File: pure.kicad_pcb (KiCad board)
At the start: 2 copper layers, 100 x 90 mm, 46 parts, among them K1 G5V-2_Split, Q1 DTC143Z, U1 SN74LVC1G3157DBVR, U2 SN74LVC1G3157DBVR, U3 74HC4053, U4 74HC4053, U5 MC33079

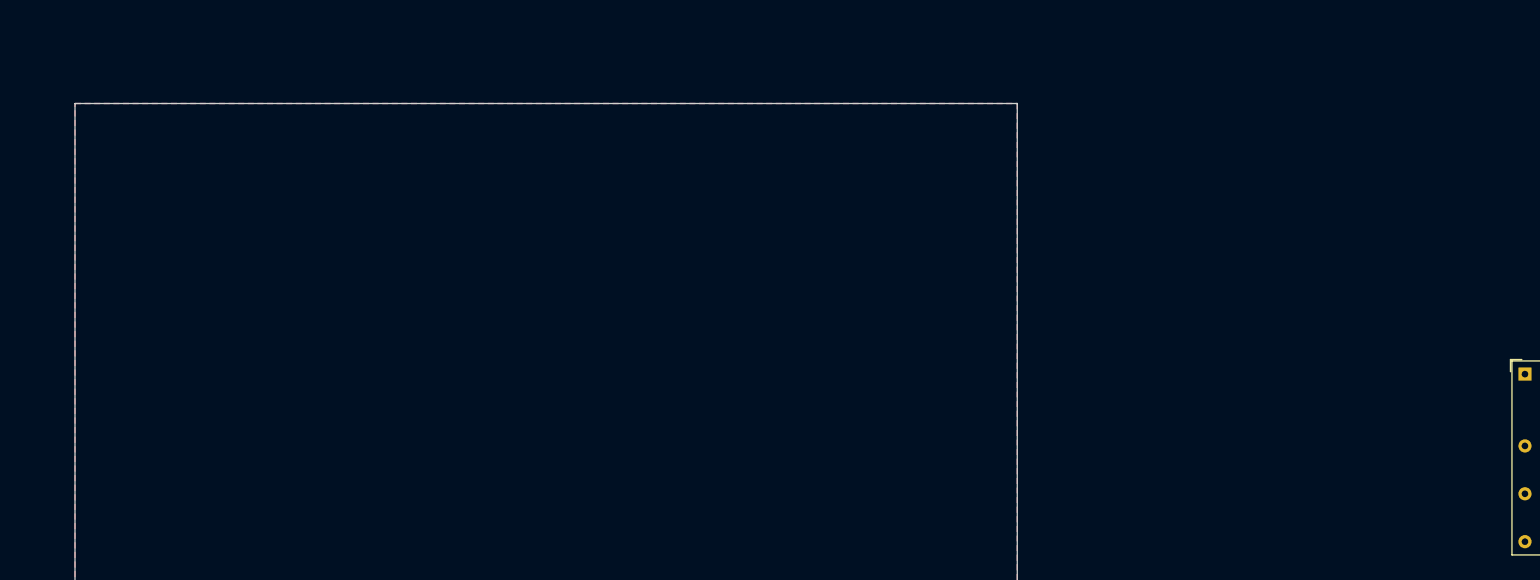
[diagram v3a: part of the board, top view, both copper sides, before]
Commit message: finich IF_RX_Schematics, begin MCU, delete *.sch files
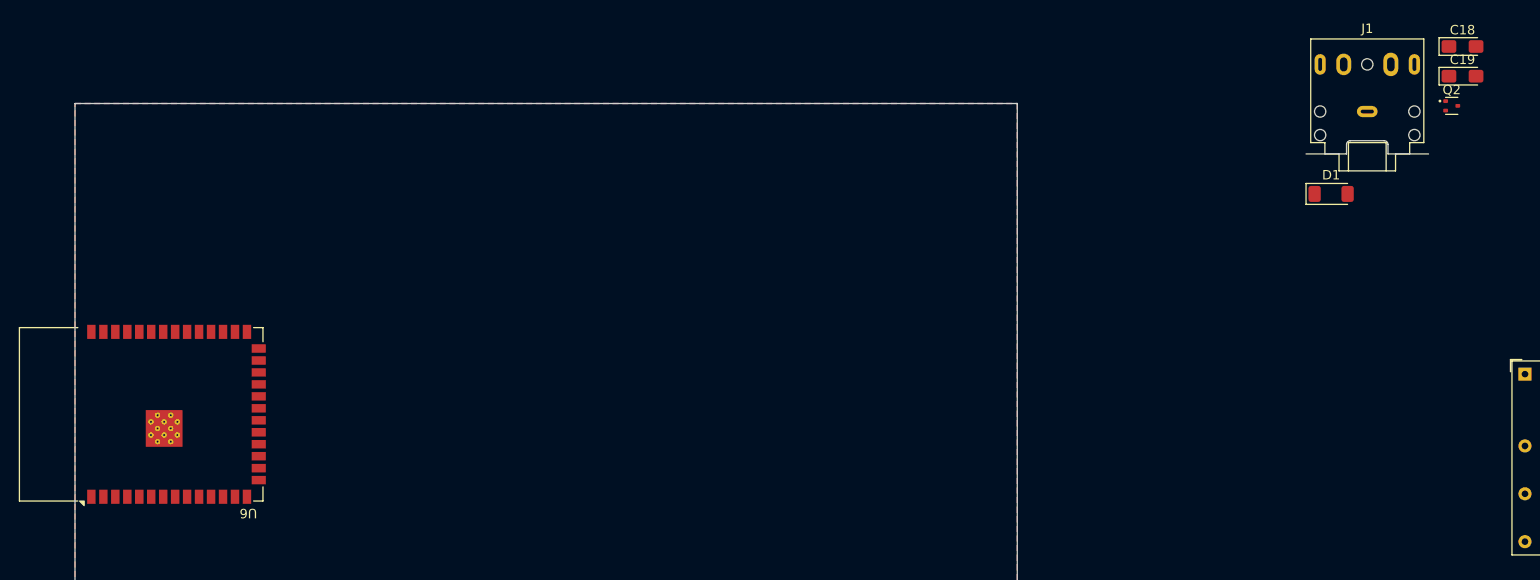
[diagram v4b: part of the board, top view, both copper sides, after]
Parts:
- added C18: 10uF, Capacitor_Tantalum_SMD:CP_EIA-3216-18_Kemet-A_Pad1.58x1.35mm_HandSolder, F.Cu at (212.2, 34.0)
- added C19: 10uF, Capacitor_Tantalum_SMD:CP_EIA-3216-18_Kemet-A_Pad1.58x1.35mm_HandSolder, F.Cu at (212.2, 37.1)
- added D1: LL4148, Diode_SMD:D_MiniMELF, F.Cu at (198.3, 49.6)
- added J1: LINE_IN, Connector_Audio:Jack_3.5mm_CUI_SJ1-3525N_Horizontal, F.Cu at (202.1, 40.9)
- added Q2: DTC143Z, Package_TO_SOT_SMD:SOT-523, F.Cu at (211.1, 40.2)
- added U6: ESP32-S3-WROOM-1, RF_Module:ESP32-S3-WROOM-1, F.Cu at (72.0, 73.0)
- K1: value G5V-2_Split -> RS-12
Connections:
- net Net-(R18-Pad1) renamed R_LINE_IN
- net Net-(R8-Pad2) renamed L_LINE_IN
- K1 pad 1: unconnected-(K1-Pad1) -> +12V
- K1 pad 16: unconnected-(K1-Pad16) -> Net-(D1-A)

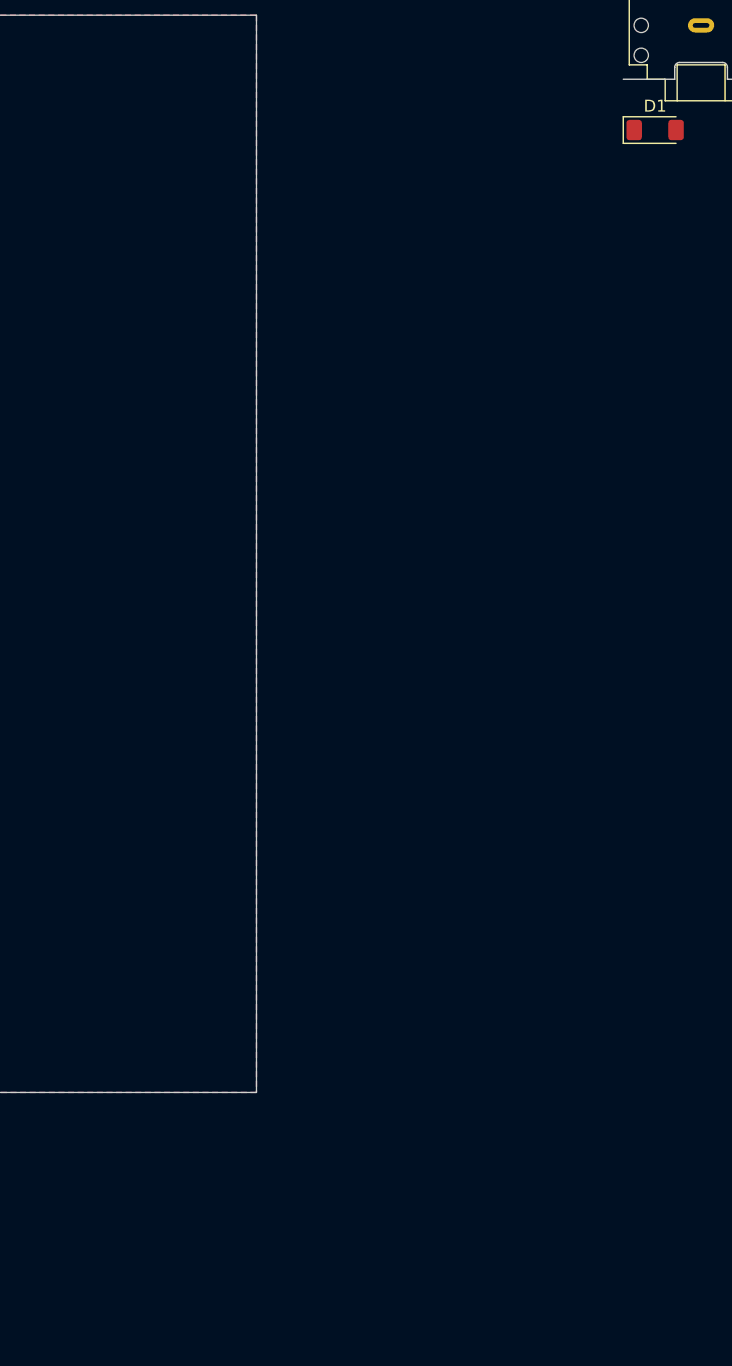
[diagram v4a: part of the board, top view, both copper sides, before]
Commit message: schematics mixer progress, mcu
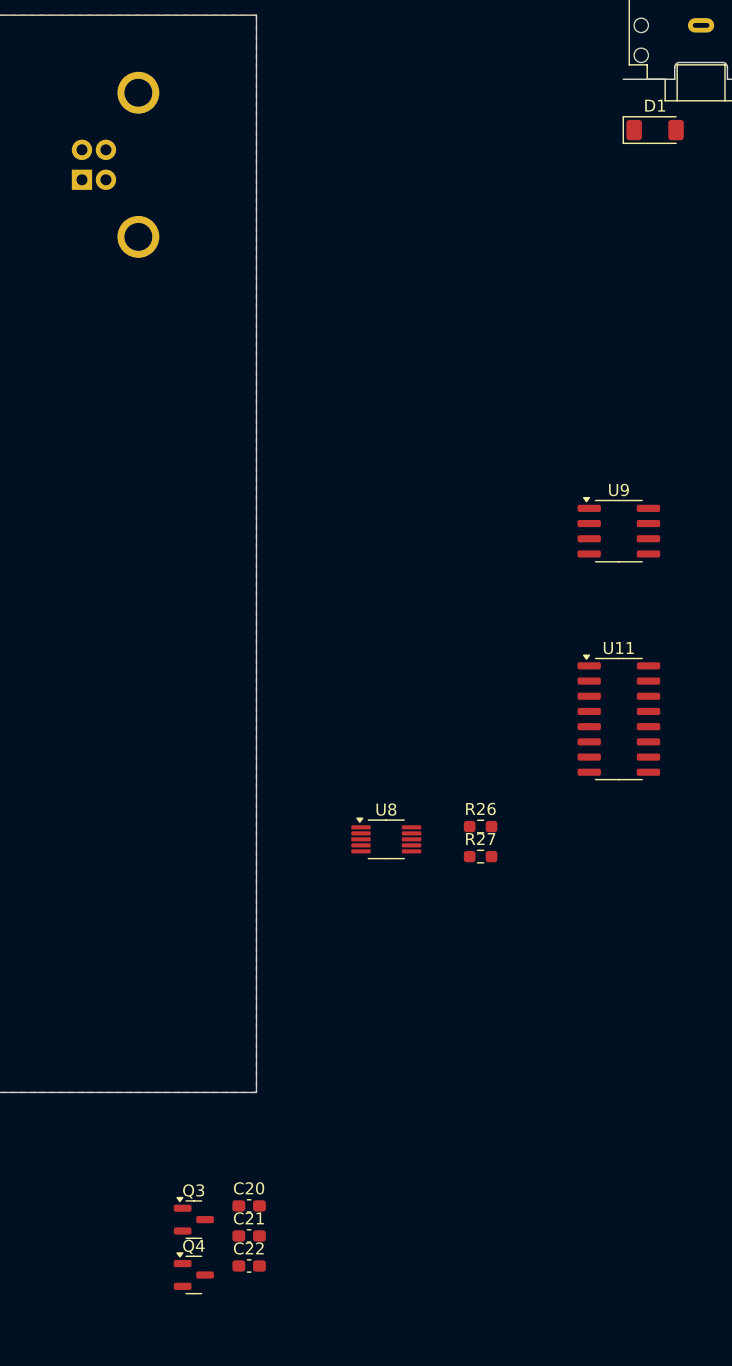
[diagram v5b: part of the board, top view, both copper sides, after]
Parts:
- added C20: 1uF, Capacitor_SMD:C_0603_1608Metric_Pad1.08x0.95mm_HandSolder, F.Cu at (164.4, 139.5)
- added C21: 100nF, Capacitor_SMD:C_0603_1608Metric_Pad1.08x0.95mm_HandSolder, F.Cu at (164.4, 142.0)
- added C22: 100nF, Capacitor_SMD:C_0603_1608Metric_Pad1.08x0.95mm_HandSolder, F.Cu at (164.4, 144.5)
- added J2: USB_B, Connector_USB:USB_B_OST_USB-B1HSxx_Horizontal, B.Cu at (150.4, 53.8)
- added Q3: BSS138, Package_TO_SOT_SMD:SOT-23, F.Cu at (159.8, 140.6)
- added Q4: BSS138, Package_TO_SOT_SMD:SOT-23, F.Cu at (159.8, 145.2)
- added R26: 10k, Resistor_SMD:R_0603_1608Metric_Pad0.98x0.95mm_HandSolder, F.Cu at (183.7, 107.8)
- added R27: 10k, Resistor_SMD:R_0603_1608Metric_Pad0.98x0.95mm_HandSolder, F.Cu at (183.7, 110.3)
- added U11: CH340C, Package_SO:SOIC-16_3.9x9.9mm_P1.27mm, F.Cu at (195.3, 98.8)
- added U8: Si5351A-B-GT, Package_SO:MSOP-10_3x3mm_P0.5mm, F.Cu at (175.8, 108.9)
- added U9: M24C01-WMN, Package_SO:SOIC-8_3.9x4.9mm_P1.27mm, F.Cu at (195.3, 83.1)
- U6: value ESP32-S3-WROOM-1 -> ESP32-S3-WROOM-1-N16R8
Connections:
- L1 pad 1: +3.3V -> +3.3VA
- R5 pad 1: +3.3V -> +3.3VA
- U6 pad 1: Net-(U6-GND-Pad1) -> GND
- U6 pad 2: unconnected-(U6-3V3-Pad2) -> +3.3V
- U6 pad 27: unconnected-(U6-IO0-Pad27) -> ESP32_IO0
- U6 pad 3: unconnected-(U6-EN-Pad3) -> ESP32_EN
- U6 pad 34: unconnected-(U6-IO41-Pad34) -> I2C_SDA
- U6 pad 35: unconnected-(U6-IO42-Pad35) -> I2C_SCL
- U6 pad 36: unconnected-(U6-RXD0-Pad36) -> UART0_RX
- U6 pad 37: unconnected-(U6-TXD0-Pad37) -> UART0_TX
- U6 pad 40: Net-(U6-GND-Pad1) -> GND
- U6 pad 41: Net-(U6-GND-Pad1) -> GND

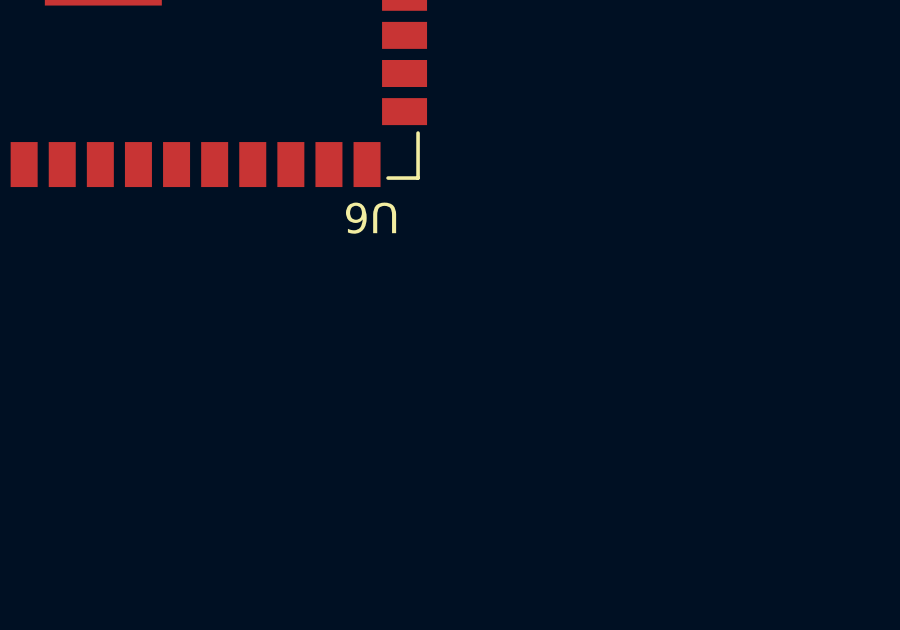
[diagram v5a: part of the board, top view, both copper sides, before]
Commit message: add BPF, add Firmware
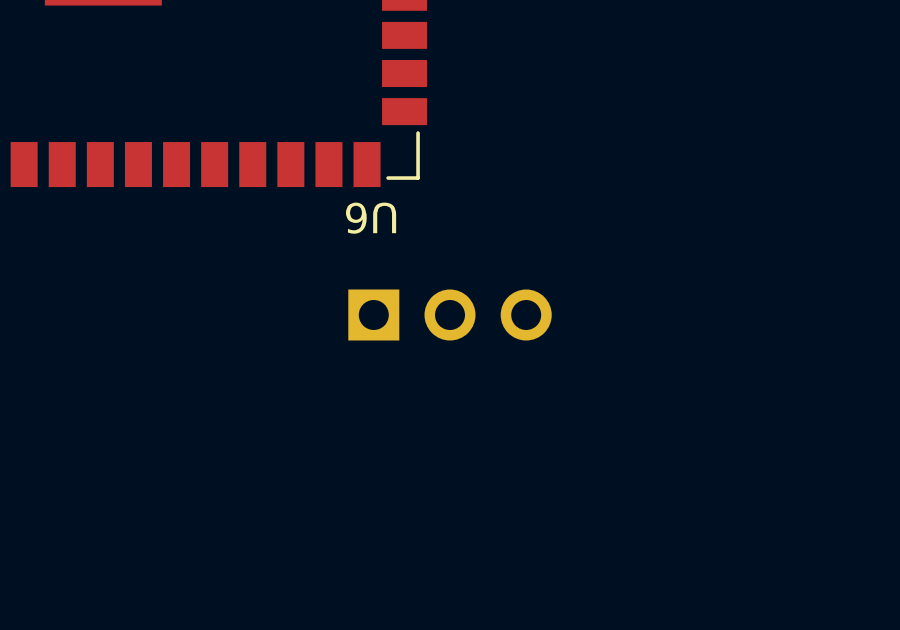
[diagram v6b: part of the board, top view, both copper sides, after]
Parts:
- added J3: Program_USB_JTAG, Connector_PinHeader_2.54mm:PinHeader_1x03_P2.54mm_Vertical, B.Cu at (83.5, 86.8)
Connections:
- U6 pad 12: unconnected-(U6-IO8-Pad12) -> KEYBOARD3
- U6 pad 13: unconnected-(U6-IO19-Pad13) -> USB_D-
- U6 pad 14: unconnected-(U6-IO20-Pad14) -> USB_D+
- U6 pad 15: unconnected-(U6-IO3-Pad15) -> LCD1602_IO3
- U6 pad 17: unconnected-(U6-IO9-Pad17) -> KEYBOARD4
- U6 pad 18: unconnected-(U6-IO10-Pad18) -> ENCODER_A
- U6 pad 19: unconnected-(U6-IO11-Pad19) -> ENCODER_B
- U6 pad 24: unconnected-(U6-IO47-Pad24) -> PREAMP
- U6 pad 25: unconnected-(U6-IO48-Pad25) -> EEPROM_WP
- U6 pad 34: I2C_SDA -> I2C_SCL
- U6 pad 35: I2C_SCL -> I2C_SDA
- U6 pad 38: unconnected-(U6-IO2-Pad38) -> LCD1602_IO2
- U6 pad 39: unconnected-(U6-IO1-Pad39) -> LCD1602_IO1
- U6 pad 4: unconnected-(U6-IO4-Pad4) -> CW_Key_DOT
- U6 pad 5: unconnected-(U6-IO5-Pad5) -> CW_Key_DACH
- U6 pad 6: unconnected-(U6-IO6-Pad6) -> KEYBOARD1
- U6 pad 7: unconnected-(U6-IO7-Pad7) -> KEYBOARD2
- U9 pad 1: unconnected-(U9-E0-Pad1) -> GND
- U9 pad 2: unconnected-(U9-E1-Pad2) -> GND
- U9 pad 3: unconnected-(U9-E2-Pad3) -> GND
- U9 pad 7: unconnected-(U9-~{WC}-Pad7) -> EEPROM_WP

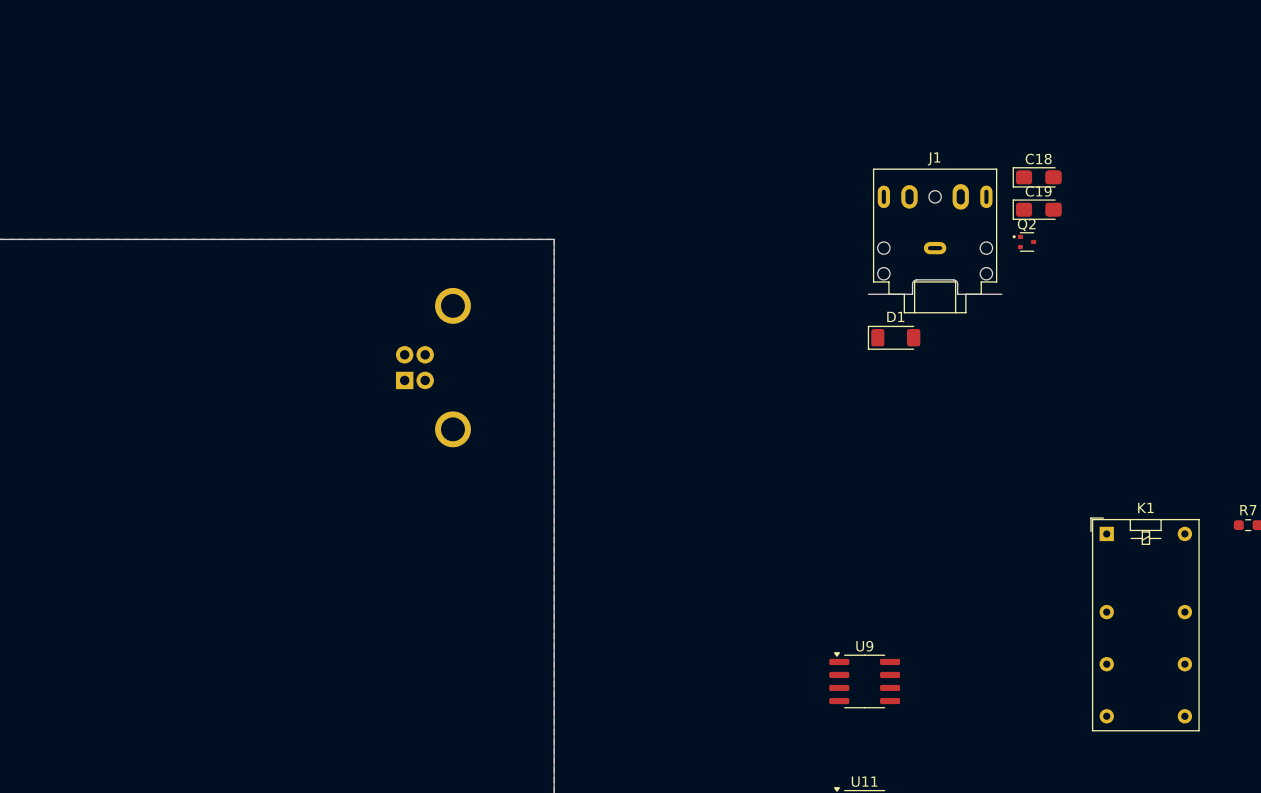
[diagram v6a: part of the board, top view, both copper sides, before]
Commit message: 10_17M BPF done
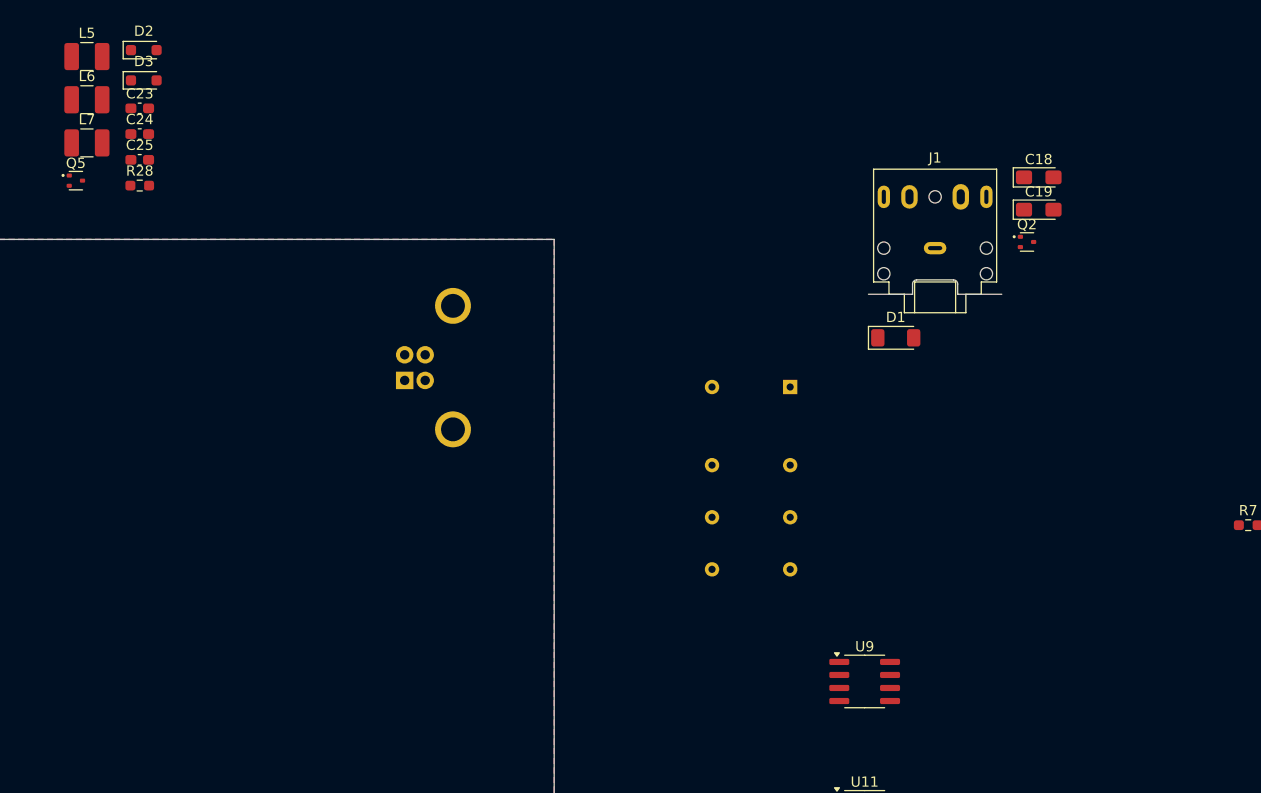
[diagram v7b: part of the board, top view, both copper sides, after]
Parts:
- added C23: 270, Capacitor_SMD:C_0603_1608Metric_Pad1.08x0.95mm_HandSolder, F.Cu at (124.6, 27.2)
- added C24: 270, Capacitor_SMD:C_0603_1608Metric_Pad1.08x0.95mm_HandSolder, F.Cu at (124.6, 29.7)
- added C25: 120, Capacitor_SMD:C_0603_1608Metric_Pad1.08x0.95mm_HandSolder, F.Cu at (124.6, 32.2)
- added D2: BAP50-03, Diode_SMD:D_SOD-323_HandSoldering, F.Cu at (125.0, 21.5)
- added D3: BAP50-03, Diode_SMD:D_SOD-323_HandSoldering, F.Cu at (125.0, 24.5)
- added L5: 0,22uH, Inductor_SMD:L_1210_3225Metric_Pad1.42x2.65mm_HandSolder, F.Cu at (119.4, 22.2)
- added L6: 0,22uH, Inductor_SMD:L_1210_3225Metric_Pad1.42x2.65mm_HandSolder, F.Cu at (119.4, 26.4)
- added L7: 0,47uH, Inductor_SMD:L_1210_3225Metric_Pad1.42x2.65mm_HandSolder, F.Cu at (119.4, 30.6)
- added Q5: DTC143Z, Package_TO_SOT_SMD:SOT-523, F.Cu at (118.4, 34.3)
- added R28: 10k, Resistor_SMD:R_0603_1608Metric_Pad0.98x0.95mm_HandSolder, F.Cu at (124.6, 34.8)
- K1: moved to B.Cu
- moved K1 34.0 mm to (188.0, 54.4), turned to 180 degrees
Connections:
- C13 pad 1: BPF -> BPF_OUT
- U6 pad 16: unconnected-(U6-IO46-Pad16) -> 74HC4053_RX_TX
